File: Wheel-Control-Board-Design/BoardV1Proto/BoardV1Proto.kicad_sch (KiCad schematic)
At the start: 14 parts

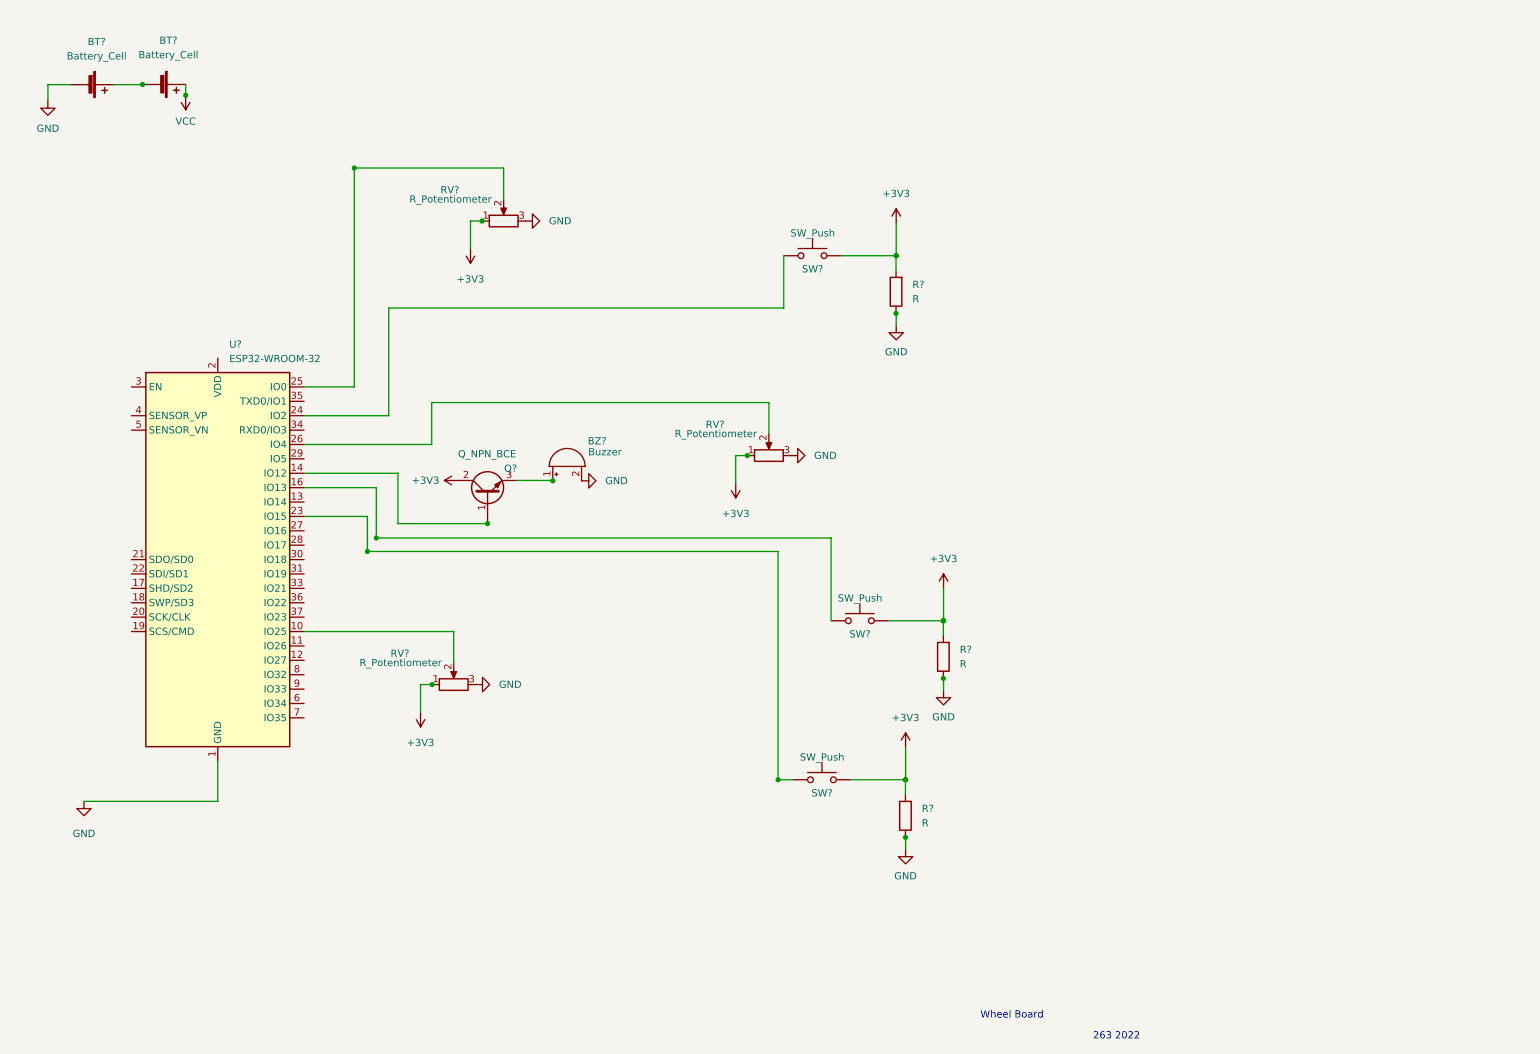
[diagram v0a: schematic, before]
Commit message: Added lin reg and more
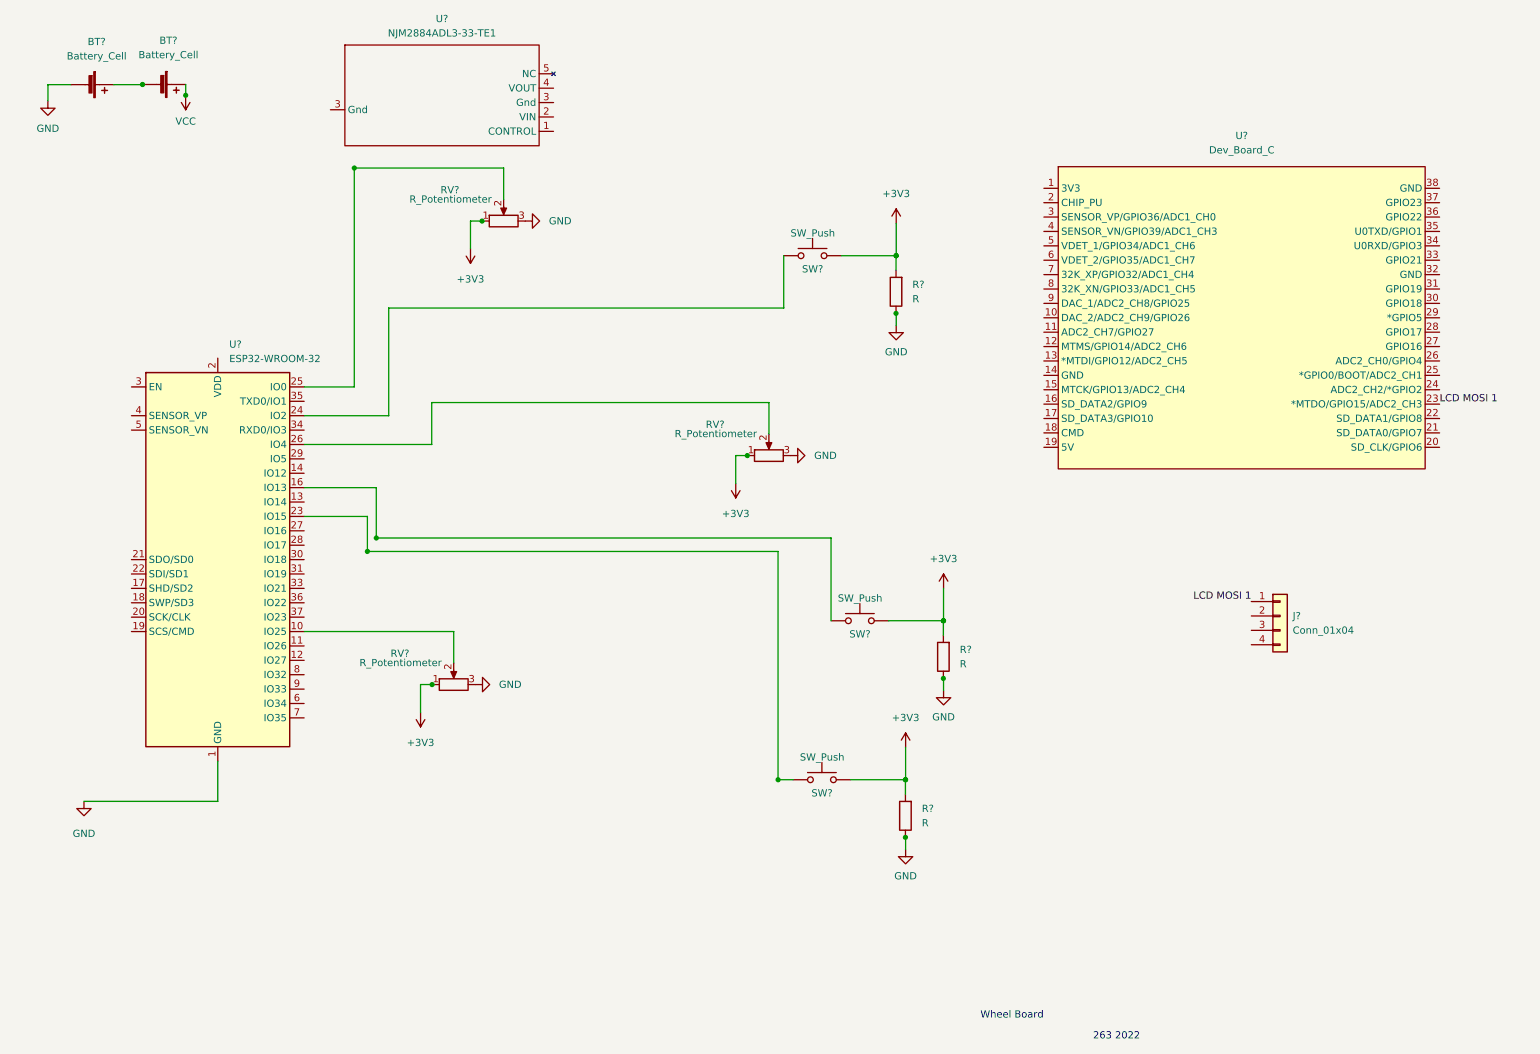
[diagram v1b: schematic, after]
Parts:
- removed BZ?: Buzzer, symbol Device:Buzzer
- removed Q?: Q_NPN_BCE, symbol Device:Q_NPN_BCE
- added J?: Conn_01x04, symbol Connector_Generic:Conn_01x04
- added U?: Dev_Board_C, symbol AERO_Symbols:Dev_Board_C
- added U?: NJM2884ADL3-33-TE1, symbol AERO_Symbols:NJM2884ADL3-33-TE1
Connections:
- new net LCD MOSI 1: J?.1 (Pin_1), U?.23 (*MTDO/GPIO15/ADC2_CH3)
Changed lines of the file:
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@@
   (junction (at 180.9087 119.9123) (diameter 0) (color 0 0 0 0)
   )
-  (junction (at 111.9617 95.2095) (diameter 0) (color 0 0 0 0)
-  )
   (junction (at 47.1558 27.159) (diameter 0) (color 0 0 0 0)
   )
@@
   (junction (at 76.9221 39.9932) (diameter 0) (color 0 0 0 0)
   )
-  (junction (at 100.4484 102.7628) (diameter 0) (color 0 0 0 0)
-  )
   (junction (at 90.6632 131.1746) (diameter 0) (color 0 0 0 0)
   )
@@
     (stroke (width 0) (type default) (color 0 0 0 0))
   )
-  (wire (pts (xy 84.6299 102.7628) (xy 100.4484 102.7628))
-    (stroke (width 0) (type default) (color 0 0 0 0))
-  )
   (wire (pts (xy 80.804 105.3009) (xy 161.0907 105.3009))
     (stroke (width 0) (type default) (color 0 0 0 0))
@@
     (stroke (width 0) (type default) (color 0 0 0 0))
   )
-  (wire (pts (xy 100.4484 102.7511) (xy 100.4484 102.7628))
-    (stroke (width 0) (type default) (color 0 0 0 0))
-  )
   (wire (pts (xy 164.5512 147.9742) (xy 174.2092 147.9742))
     (stroke (width 0) (type default) (color 0 0 0 0))
@@
     (stroke (width 0) (type default) (color 0 0 0 0))
   )
-  (wire (pts (xy 111.9617 95.1428) (xy 111.9617 95.2095))
-    (stroke (width 0) (type default) (color 0 0 0 0))
-  )
   (wire (pts (xy 68.0679 121.8144) (xy 94.4732 121.8144))
     (stroke (width 0) (type default) (color 0 0 0 0))
@@
     (stroke (width 0) (type default) (color 0 0 0 0))
   )
-  (wire (pts (xy 68.0679 93.8744) (xy 84.6299 93.8744))
-    (stroke (width 0) (type default) (color 0 0 0 0))
-  )
   (wire (pts (xy 88.6185 136.0914) (xy 88.6185 131.1701))
     (stroke (width 0) (type default) (color 0 0 0 0))
@@
     (stroke (width 0) (type default) (color 0 0 0 0))
   )
-  (wire (pts (xy 84.6299 93.8744) (xy 84.6299 102.7628))
-    (stroke (width 0) (type default) (color 0 0 0 0))
-  )
   (wire (pts (xy 68.0679 88.7944) (xy 90.589 88.7944))
     (stroke (width 0) (type default) (color 0 0 0 0))
@@
   )
   (wire (pts (xy 172.5829 65.6467) (xy 172.5511 65.6467))
-    (stroke (width 0) (type default) (color 0 0 0 0))
-  )
-  (wire (pts (xy 105.5284 95.1428) (xy 111.9617 95.1428))
     (stroke (width 0) (type default) (color 0 0 0 0))
   )
@@
     (effects (font (size 1.27 1.27)) (justify left bottom))
   )
+  (label "LCD MOSI 1" (at 268.4982 81.6693 0)
+    (effects (font (size 1.27 1.27)) (justify left bottom))
+  )
+  (label "LCD MOSI 1" (at 235.2672 116.5209 180)
+    (effects (font (size 1.27 1.27)) (justify right bottom))
+  )
   (symbol (lib_id "power:VCC") (at 47.1558 27.159 180) (unit 1)
     (in_bom yes) (on_board yes) (fields_autoplaced)
@@
     )
     (property "Datasheet" "" (id 3) (at 47.1558 27.159 0)
-      (effects (font (size 1.27 1.27)) hide)
-    )
-    (pin "1")
-  )
-  (symbol (lib_id "power:+3V3") (at 95.3684 95.1428 90) (unit 1)
-    (in_bom yes) (on_board yes) (fields_autoplaced)
-    (property "Reference" "#PWR?" (id 0) (at 99.1784 95.1428 0)
-      (effects (font (size 1.27 1.27)) hide)
-    )
-    (property "Value" "+3V3" (id 1) (at 91.9375 95.1427 90)
-      (effects (font (size 1.27 1.27)) (justify left))
-    )
-    (property "Footprint" "" (id 2) (at 95.3684 95.1428 0)
-      (effects (font (size 1.27 1.27)) hide)
-    )
-    (property "Datasheet" "" (id 3) (at 95.3684 95.1428 0)
       (effects (font (size 1.27 1.27)) hide)
     )
@@
     )
     (pin "1")
+  )
+  (symbol (lib_id "AERO_Symbols:Dev_Board_C") (at 235.4782 70.2393 0) (unit 1)
+    (in_bom yes) (on_board yes) (fields_autoplaced)
+    (property "Reference" "U?" (id 0) (at 233.5732 34.29 0))
+    (property "Value" "Dev_Board_C" (id 1) (at 233.5732 36.83 0))
+    (property "Footprint" "" (id 2) (at 235.4782 70.2393 0)
+      (effects (font (size 1.27 1.27)) hide)
+    )
+    (property "Datasheet" "" (id 3) (at 235.4782 70.2393 0)
+      (effects (font (size 1.27 1.27)) hide)
+    )
+    (pin "14")
+    (pin "19")
+    (pin "1")
+    (pin "10")
+    (pin "11")
+    (pin "12")
+    (pin "13")
+    (pin "15")
+    (pin "16")
+    (pin "17")
+    (pin "18")
+    (pin "2")
+    (pin "20")
+    (pin "21")
+    (pin "22")
+    (pin "23")
+    (pin "24")
+    (pin "25")
+    (pin "26")
+    (pin "27")
+    (pin "28")
+    (pin "29")
+    (pin "3")
+    (pin "30")
+    (pin "31")
+    (pin "32")
+    (pin "33")
+    (pin "34")
+    (pin "35")
+    (pin "36")
+    (pin "37")
+    (pin "38")
+    (pin "4")
+    (pin "5")
+    (pin "6")
+    (pin "7")
+    (pin "8")
+    (pin "9")
   )
   (symbol (lib_id "Switch:SW_Push") (at 159.4712 147.9742 0) (unit 1)
@@
     (pin "3")
   )
+  (symbol (lib_id "AERO_Symbols:NJM2884ADL3-33-TE1") (at 91.7695 24.6276 0) (unit 1)
+    (in_bom yes) (on_board yes) (fields_autoplaced)
+    (property "Reference" "U?" (id 0) (at 92.4045 13.647 0))
+    (property "Value" "NJM2884ADL3-33-TE1" (id 1) (at 92.4045 16.187 0))
+    (property "Footprint" "" (id 2) (at 86.6895 27.1676 0)
+      (effects (font (size 1.27 1.27)) hide)
+    )
+    (property "Datasheet" "" (id 3) (at 86.6895 27.1676 0)
+      (effects (font (size 1.27 1.27)) hide)
+    )
+    (pin "1")
+    (pin "2")
+    (pin "3")
+    (pin "3")
+    (pin "4")
+    (pin "5")
+  )
   (symbol (lib_id "Device:Battery_Cell") (at 29.4178 25.2759 270) (unit 1)
     (in_bom yes) (on_board yes) (fields_autoplaced)
@@
     (pin "1")
   )
+  (symbol (lib_id "Connector_Generic:Conn_01x04") (at 240.3472 119.0609 0) (unit 1)
+    (in_bom yes) (on_board yes) (fields_autoplaced)
+    (property "Reference" "J?" (id 0) (at 242.57 119.0608 0)
+      (effects (font (size 1.27 1.27)) (justify left))
+    )
+    (property "Value" "Conn_01x04" (id 1) (at 242.57 121.6008 0)
+      (effects (font (size 1.27 1.27)) (justify left))
+    )
+    (property "Footprint" "" (id 2) (at 240.3472 119.0609 0)
+      (effects (font (size 1.27 1.27)) hide)
+    )
+    (property "Datasheet" "~" (id 3) (at 240.3472 119.0609 0)
+      (effects (font (size 1.27 1.27)) hide)
+    )
+    (pin "1")
+    (pin "2")
+    (pin "3")
+    (pin "4")
+  )
   (symbol (lib_id "Device:R") (at 172.5511 61.8367 180) (unit 1)
     (in_bom yes) (on_board yes) (fields_autoplaced)
@@
     )
     (property "Datasheet" "" (id 3) (at 172.5829 67.7821 0)
-      (effects (font (size 1.27 1.27)) hide)
-    )
-    (pin "1")
-  )
-  (symbol (lib_id "power:GND") (at 117.0417 95.2095 90) (unit 1)
-    (in_bom yes) (on_board yes) (fields_autoplaced)
-    (property "Reference" "#PWR?" (id 0) (at 123.3917 95.2095 0)
-      (effects (font (size 1.27 1.27)) hide)
-    )
-    (property "Value" "GND" (id 1) (at 121.2147 95.2094 90)
-      (effects (font (size 1.27 1.27)) (justify right))
-    )
-    (property "Footprint" "" (id 2) (at 117.0417 95.2095 0)
-      (effects (font (size 1.27 1.27)) hide)
-    )
-    (property "Datasheet" "" (id 3) (at 117.0417 95.2095 0)
       (effects (font (size 1.27 1.27)) hide)
     )
@@
     )
     (property "Datasheet" "~" (id 3) (at 43.6081 25.2466 90)
-      (effects (font (size 1.27 1.27)) hide)
-    )
-    (pin "1")
-    (pin "2")
-  )
-  (symbol (lib_id "Device:Buzzer") (at 114.5017 92.6695 90) (unit 1)
-    (in_bom yes) (on_board yes)
-    (property "Reference" "BZ?" (id 0) (at 118.1451 88.1954 90)
-      (effects (font (size 1.27 1.27)) (justify right))
-    )
-    (property "Value" "Buzzer" (id 1) (at 118.2206 90.121 90)
-      (effects (font (size 1.27 1.27)) (justify right))
-    )
-    (property "Footprint" "" (id 2) (at 111.9617 93.3045 90)
-      (effects (font (size 1.27 1.27)) hide)
-    )
-    (property "Datasheet" "~" (id 3) (at 111.9617 93.3045 90)
       (effects (font (size 1.27 1.27)) hide)
     )
@@
     (pin "2")
   )
-  (symbol (lib_id "Device:Q_NPN_BCE") (at 100.4484 97.6828 90) (unit 1)
-    (in_bom yes) (on_board yes)
-    (property "Reference" "Q?" (id 0) (at 105.662 93.0252 90)
-      (effects (font (size 1.27 1.27)) (justify left))
-    )
-    (property "Value" "Q_NPN_BCE" (id 1) (at 105.5076 90.4714 90)
-      (effects (font (size 1.27 1.27)) (justify left))
-    )
-    (property "Footprint" "" (id 2) (at 97.9084 92.6028 0)
-      (effects (font (size 1.27 1.27)) hide)
-    )
-    (property "Datasheet" "~" (id 3) (at 100.4484 97.6828 0)
-      (effects (font (size 1.27 1.27)) hide)
-    )
-    (pin "1")
-    (pin "2")
-    (pin "3")
-  )
   (symbol (lib_id "power:GND") (at 174.241 160.2852 0) (unit 1)
     (in_bom yes) (on_board yes) (fields_autoplaced)
@@
       (reference "#PWR?") (unit 1) (value "VCC") (footprint "")
     )
-    (path "/0829a55c-3af6-44b1-ace4-a637921a1181"
-      (reference "#PWR?") (unit 1) (value "+3V3") (footprint "")
-    )
     (path "/0ea59a30-84db-4aac-a37d-d423466a18b6"
       (reference "#PWR?") (unit 1) (value "GND") (footprint "")
@@
       (reference "#PWR?") (unit 1) (value "GND") (footprint "")
     )
-    (path "/8cc246ef-a9d3-43c8-a2b3-a6d0c0a31a25"
-      (reference "#PWR?") (unit 1) (value "GND") (footprint "")
-    )
     (path "/a2f5aa1d-0c39-46ed-9990-b8f90e87bcc7"
       (reference "#PWR?") (unit 1) (value "GND") (footprint "")
@@
       (reference "BT?") (unit 1) (value "Battery_Cell") (footprint "")
     )
-    (path "/90d318c9-4be0-4ab5-a8d0-90fa9dd9ca1b"
-      (reference "BZ?") (unit 1) (value "Buzzer") (footprint "")
-    )
-    (path "/d77903cf-7064-4cfa-843b-fa88cfaf7e6d"
-      (reference "Q?") (unit 1) (value "Q_NPN_BCE") (footprint "")
+    (path "/776af9b2-f46b-44c1-8858-ddb742e7ab30"
+      (reference "J?") (unit 1) (value "Conn_01x04") (footprint "")
     )
     (path "/658ad617-2838-49db-aafc-cdf95c290d8c"
@@
       (reference "SW?") (unit 1) (value "SW_Push") (footprint "")
     )
+    (path "/37ab4b37-cd58-47c7-90bf-19f635599743"
+      (reference "U?") (unit 1) (value "Dev_Board_C") (footprint "")
+    )
     (path "/3d5e3b5b-81c2-4e43-bf2b-0efd6ddc35c8"
       (reference "U?") (unit 1) (value "ESP32-WROOM-32") (footprint "RF_Module:ESP32-WROOM-32")
     )
-  )
+    (path "/4e23c26a-43e6-4d13-ac6f-b74a22c18f6a"
+      (reference "U?") (unit 1) (value "NJM2884ADL3-33-TE1") (footprint "")
+    )
+  )

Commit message: Started rework
Started reworking the board to fit new board type, added a shortcuts sheet txt so I can remember, and did some general clean up.
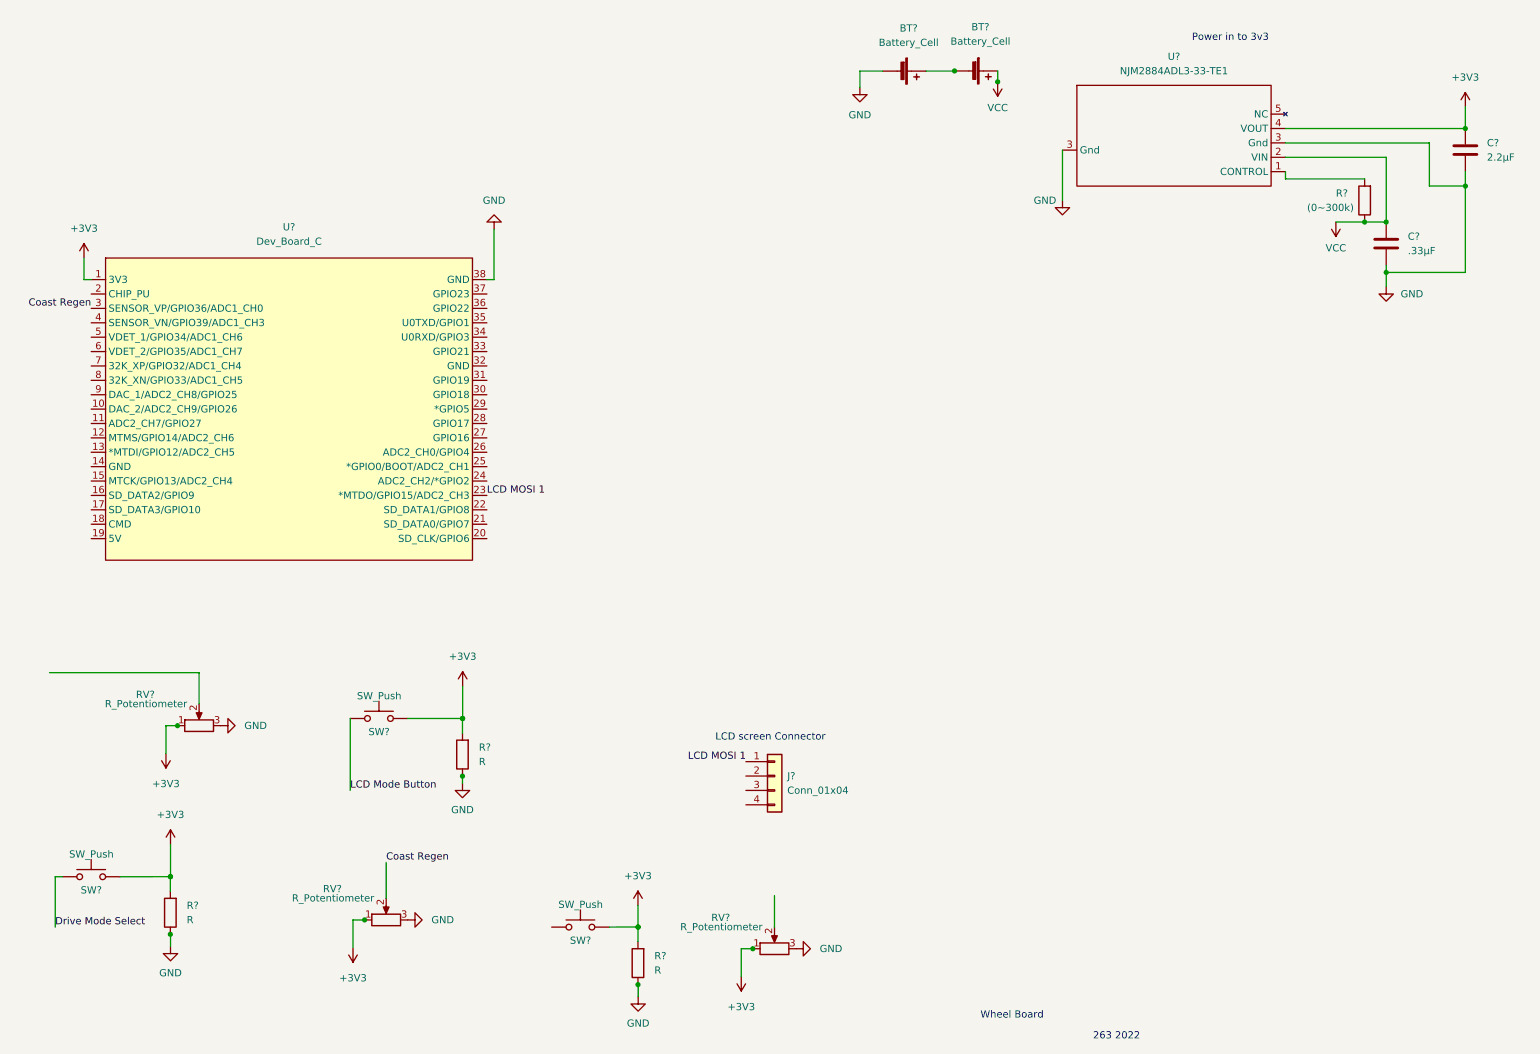
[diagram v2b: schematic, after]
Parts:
- removed U?: ESP32-WROOM-32, RF_Module:ESP32-WROOM-32, symbol RF_Module:ESP32-WROOM-32
- added C?: 2.2µF, symbol Device:C
- added C?: .33µF, symbol Device:C
- added R?: (0~300k), symbol Device:R
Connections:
- net +3V3: now also U?.1 (3V3), U?.4 (VOUT), C?.1
- net GND: now also U?.3 (Gnd), U?.38 (GND), C?.2, C?.2
- net VCC: now also U?.2 (VIN), C?.1, R?.1
- net LCD Mode Button: now reaches SW?.1
- net Coast Regen: now reaches U?.3 (SENSOR_VP/GPIO36/ADC1_CH0)
- net Coast Regen: now also RV?.2
- net Drive Mode Select: now reaches SW?.1
- net at U?.1 (CONTROL): now also R?.2
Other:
- note added: "LCD screen Connector"
- note added: "Power in to 3v3"
- moved on the sheet: BT?, J?, R?, RV?, SW?, U?
